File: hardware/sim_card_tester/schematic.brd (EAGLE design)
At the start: 160 x 100 mm, 146 parts, among them IC1 TPS6300, J2 MICRO_USB_B_HIROSE_ZX62R-B-5P, J3 CON_MICRO_SDDM3AT-SF-PEJM5, J4 NANO_SIM, J5 NANO_SIM, J6 TC2030-JLINK-NL, J7 NANO_SIM, J8 NANO_SIM, J9 U.FL-R-SMT, Q11 SI223DDS, Q3 MOSFET-NCHANNELSMD, Q4 MOSFET-NCHANNELSMD, Q5 MOSFET-NCHANNELSMD, U1 AB1815-T3, U10 SIP32510, U11 SIP32510, U14 SARA-U2, U15 MAX4734EUB+, U16 SARA-U2, U17 TXB0104RUT, U2 BGA725L6-ALT, U20 MAX4734EUB+, U21 MAX4734EUB+, U22 MAX4734EUB+, U3 FTDI234XD, U4 SAFFB1G56KB0F0A, U5 MAX8887EZK33+T, U6 MCP73831, U7 MAX-M8, U8 MAX67XXMAX6749MAX67XX, U9 NRF52840, X1 ABS07-32.768KHZ-7-T, X4 32MHz, X5 32.768kHz

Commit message: second pcb
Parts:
- removed C13: 33pF, passives:0603_CAP
- removed C15: 100uF, passives:0805_CAP
- removed C22, C24, C25, C26: 47pF, passives:0402_CAP
- removed C49: 56pF, passives:0402_CAP
- removed C50: 10nF, passives:0402_CAP
- removed C51: 100nF, passives:0402_CAP
- removed C52: 220uF, passives:1210_CAP
- removed D10, D11, D8, D9: 14V, passives:0402_DIODE
- removed J9: U.FL-R-SMT, connector:U.FL_SMT
- removed Q11: SI223DDS, fets:SOT23-3
- removed Q4, Q5: MOSFET-NCHANNELSMD, fets:SOT23-3
- removed R25: 10k, passives:0402_RES
- removed R36: 0, passives:0402_RES
- removed R40, R42: 100k, passives:0402_RES
- removed R45: 100, passives:0402_RES
- removed U14, U16: SARA-U2, ubloxLib:SARA-96
- removed U17: TXB0104RUT, chips:UQFN-12
- added C11, C12, C16, C28: 47pF, passives:0402_CAP
- added C17: 56pF, passives:0402_CAP
- added C18: 100uF, passives:0805_CAP
- added C19: 10nF, passives:0402_CAP
- added C20: 220uF, passives:1210_CAP
- added C21: 100nF, passives:0402_CAP
- added C27: 33pF, passives:0603_CAP
- added D3, D4, D6, D7: 14V, passives:0402_DIODE
- added J13: U.FL-R-SMT, connector:U.FL_SMT
- added Q2, Q6: MOSFET-NCHANNELSMD, fets:SOT23-3
- added Q7: SI223DDS, fets:SOT23-3
- added R10: 10k, passives:0402_RES
- added R43, R46: 100k, passives:0402_RES
- added R47: 0, passives:0402_RES
- added R48: 100, passives:0402_RES
- added U12: UBLOX_SARA_G350, signpost:UBLOX_SARA_G3
- added U13: TXB0104RUT, chips:UQFN-12
- moved U5 132.8 mm to (138.4, 78.7)
- moved C33 130.7 mm to (141.0, 81.3)
- moved R32 114.9 mm to (149.9, 96.5)
- moved JP1 112.4 mm to (151.1, 87.6)
- moved J2 107.0 mm to (118.1, 50.8)
- moved FB2 106.8 mm to (119.4, 61.0), turned to 90 degrees
- moved R9 102.9 mm to (61.0, 27.9)
- moved C5 94.8 mm to (115.6, 57.1)
- moved R1 93.0 mm to (110.5, 52.1)
- moved C4 85.3 mm to (110.5, 62.2)
- moved C43 84.7 mm to (25.4, 73.7)
- moved C42 81.1 mm to (20.3, 73.7)
- moved B1 79.6 mm to (120.7, 94.0)
- moved U3 75.0 mm to (105.4, 50.8), turned to 180 degrees
- moved C44 69.0 mm to (45.7, 68.6)
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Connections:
- removed net N$10: C13.2, R36.2
- removed net N$11: C13.1, U16.56
- removed net N$50: J9.SIG, R36.1
- removed net N$52: Q4.3, Q5.3, U16.9
- removed net N$54: Q4.2, U16.18
- removed net N$56: R42.2
- removed net N$57: Q5.2, U16.15
- removed net N$58: U16.10, U17.2
- removed net N$62: U16.11, U17.3
- removed net N$7: R25.1, U17.12
- removed net N$80: Q11.1, R45.1
- removed net N$95: C22.2, C24.2, C25.2, C26.2, D10.ANODE, D11.ANODE, D8.ANODE, D9.ANODE
- removed net RXD: U16.13, U17.5
- removed net TXD: U16.12, U17.4
- removed net VBCKP: C15.P$1, R42.1, U14.2
- removed net VSIM: U16.41
- removed net V_BCKP: U16.2
- removed net V_INT: U16.4
- new net 3V3: R10.2, U13.11
- new net N$12: U12.13, U13.5
- new net N$15: Q6.3, U12.18
- new net N$16: C18.P$1, R43.2, U12.2
- new net N$18: Q2.3, R43.1, U12.15
- new net N$25: U12.11, U13.3
- new net N$53: U12.10, U13.2
- new net N$63: C27.2, R47.1
- new net N$66: Q7.1, R48.1
- new net N$68: R10.1, U13.12
- new net N$69: C27.1, U12.56
- new net N$70: J13.SIG, R47.2
- new net N$71: C11.2, C12.2, C16.2, C28.2, D3.ANODE, D4.ANODE, D6.ANODE, D7.ANODE
- new net N$9: U12.12, U13.4
- net +3V3: no longer R25.2, U17.11
- net CLK_SIM: now also C28.1, D7.CATHODE, U12.38; no longer C26.1, D11.CATHODE, U14.38
- net GND: now also C17.2, C18.P$2, C19.2, C20.2, C21.2, J13.GND1, J13.GND2, Q2.2, Q6.2, R46.1, U12.1, U12.14, U12.20, U12.21, U12.22, U12.3, U12.30, U12.32, U12.33, U12.43, U12.5, U12.50, U12.54, U12.55, U12.57, U12.58, U12.59, U12.60, U12.61, U12.63, U12.64, U12.65, U12.66, U12.67, U12.68, U12.69, U12.70, U12.71, U12.72, U12.73, U12.74, U12.75, U12.76, U12.77, U12.78, U12.79, U12.80, U12.81, U12.82, U12.83, U12.84, U12.85, U12.86, U12.87, U12.88, U12.89, U12.9, U12.90, U12.91, U12.92, U12.93, U12.94, U12.95, U12.96, U13.6; no longer C15.P$2, C49.2, C50.2, C51.2, C52.2, J9.GND1, J9.GND2, R40.1, U14.1, U14.14, U14.20, U14.21, U14.22, U14.3, U14.30, U14.32, U14.43, U14.5, U14.50, U14.54, U14.55, U14.57, U14.58, U14.59, U14.60, U14.61, U14.63, U14.64, U14.65, U14.66, U14.67, U14.68, U14.69, U14.70, U14.71, U14.72, U14.73, U14.74, U14.75, U14.76, U14.77, U14.78, U14.79, U14.80, U14.81, U14.82, U14.83, U14.84, U14.85, U14.86, U14.87, U14.88, U14.89, U14.90, U14.91, U14.92, U14.93, U14.94, U14.95, U14.96, U16.1, U16.14, U16.20, U16.21, U16.22, U16.3, U16.30, U16.32, U16.43, U16.5, U16.50, U16.54, U16.55, U16.57, U16.58, U16.59, U16.60, U16.61, U16.63, U16.64, U16.65, U16.66, U16.67, U16.68, U16.69, U16.70, U16.71, U16.72, U16.73, U16.74, U16.75, U16.76, U16.77, U16.78, U16.79, U16.80, U16.81, U16.82, U16.83, U16.84, U16.85, U16.86, U16.87, U16.88, U16.89, U16.90, U16.91, U16.92, U16.93, U16.94, U16.95, U16.96, U17.6
- net GSM_3V8: now also Q7.2; no longer Q11.2
- net GSM_CTS: now also U13.10; no longer U17.10
- net GSM_GATED: now also C17.1, C19.1, C20.1, C21.1, Q7.3, U12.51, U12.52, U12.53; no longer C49.1, C50.1, C51.1, C52.1, Q11.3, U14.53
- net GSM_LED: now also U12.16; no longer U16.16
- net GSM_POWER: now also Q2.1; no longer Q5.1
- net GSM_POWER_GATE: now also R46.2, R48.2; no longer R40.2, R45.2
- net GSM_RST: now also Q6.1; no longer Q4.1
- net GSM_RTS: now also U13.9; no longer U17.9
- net GSM_RX: now also U13.8; no longer U17.8
- net GSM_TX: now also U13.7; no longer U17.7
- net IO_SIM: now also C11.1, D4.CATHODE, U12.39; no longer C22.1, D9.CATHODE, U14.39
- net RST_SIM: now also C12.1, D6.CATHODE, U12.40; no longer C24.1, D10.CATHODE, U14.40
- net VCC: no longer U14.51, U14.52, U16.51, U16.52, U16.53
- net VCC_SIM: now also C16.1, D3.CATHODE, U12.41; no longer C25.1, D8.CATHODE, U14.41
- net V_GSM_INT: now also U12.4, U13.1; no longer U14.4, U17.1
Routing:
- net GND: track 1200.7 -> 0.00 mm, vias 52 -> 0
- net N$17: track 195.8 -> 5.30 mm, vias 10 -> 0
- net N$51: track 198.8 -> 32.8 mm, vias 15 -> 0
- net BAT: track 185.1 -> 35.6 mm, vias 18 -> 2
- net GPS_VCC: track 221.9 -> 77.6 mm, vias 19 -> 6
- net !SD_DETECT: track 195.6 -> 59.3 mm, vias 19 -> 0
- net WDI: track 84.0 -> 219.1 mm, vias 2 -> 5
- net VCC: track 281.3 -> 167.5 mm, vias 28 -> 8
- net !NRF_CS_SD: track 165.9 -> 52.6 mm, vias 9 -> 4
- net MUX_SEL2: track 70.9 -> 181.0 mm, vias 9 -> 12
- net D+: track 123.0 -> 17.2 mm, vias 8 -> 2
- net N$27: track 106.2 -> 5.36 mm, vias 4 -> 0
- net N$46: track 107.2 -> 7.66 mm, vias 2 -> 0
- net N$48: track 101.9 -> 3.30 mm, vias 6 -> 0
- net RXD: track 93.9 -> 0.00 mm, vias 6 -> 0
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
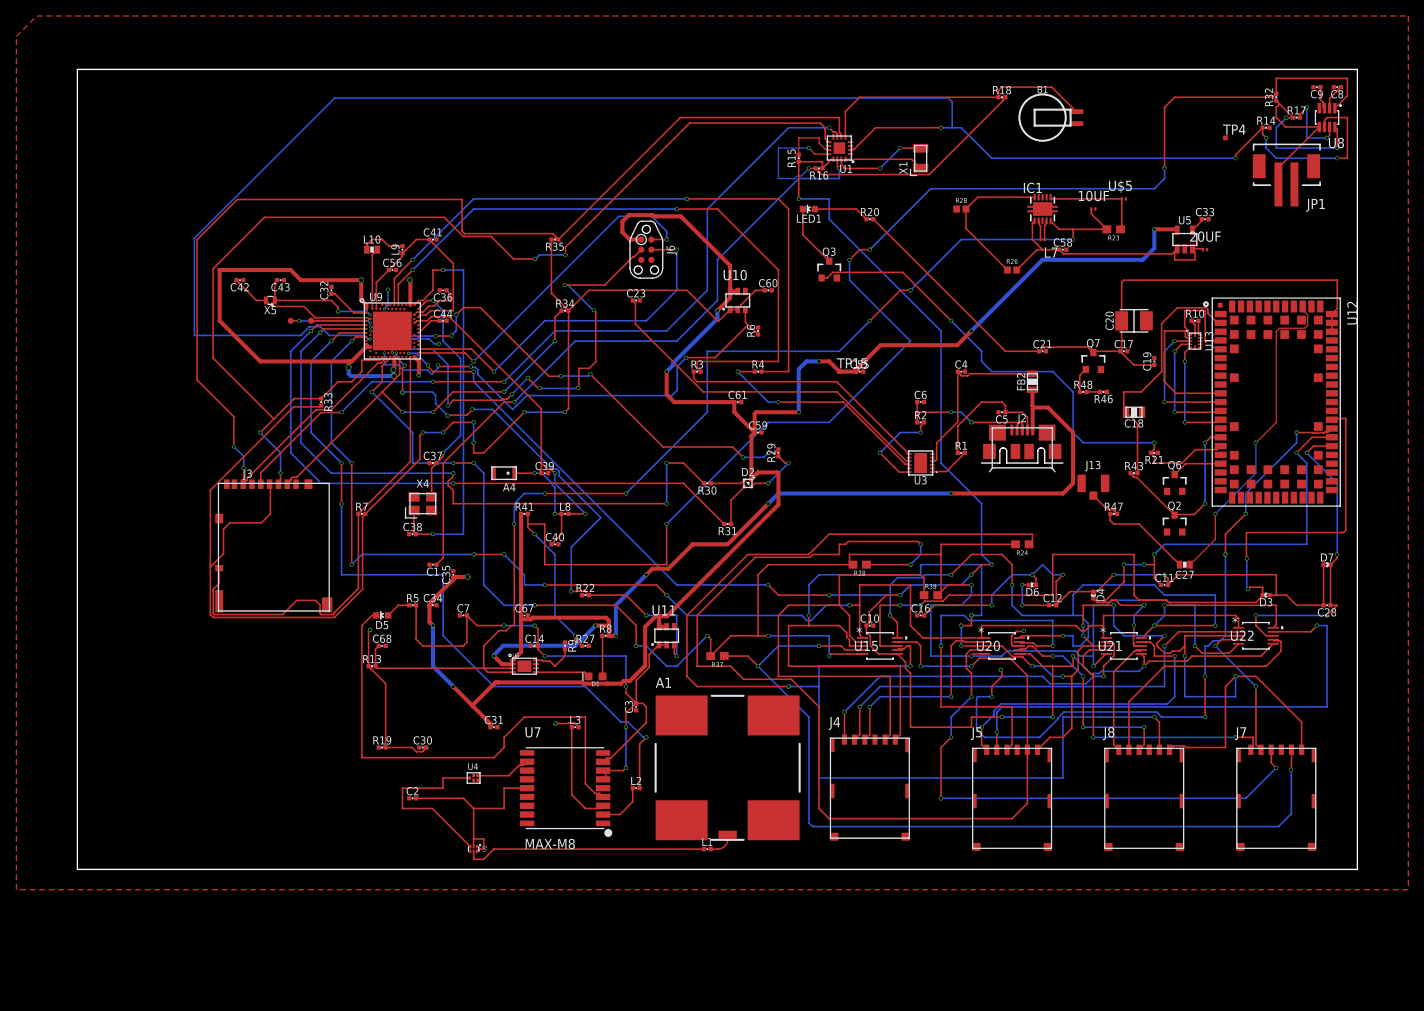
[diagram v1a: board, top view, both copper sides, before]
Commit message: fixed schematic and nrf routing
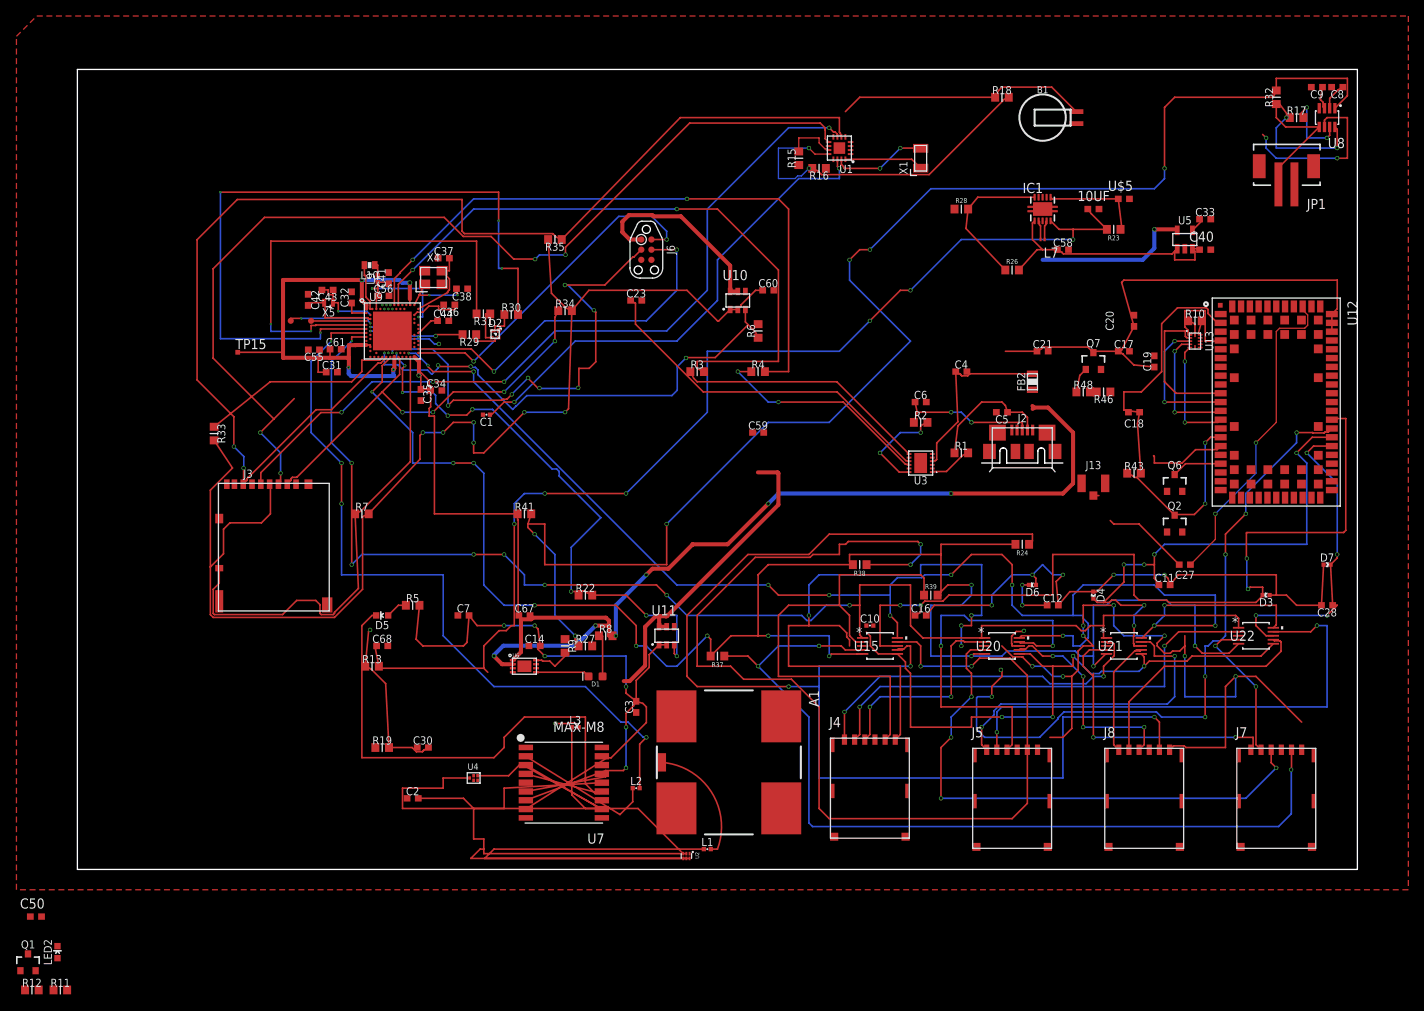
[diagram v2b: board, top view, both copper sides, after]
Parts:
- removed 20UF: (no value), Nordic_nRF:RESC0201_L
- removed A4: ANT3216A063R2400A, chips:ANT3216A063R2400A
- removed C39: 1pF, passives:0402_CAP
- removed L8: 3.9nH, passives:0402_CAP
- removed LED1: BLUE, leds:LED-0603
- removed Q3: MOSFET-NCHANNELSMD, fets:SOT23-3
- removed R14: 10k, passives:0402_RES
- removed R20: 1k, passives:0402_RES
- removed R21: 100k, passives:0402_RES
- removed R47: 0, passives:0402_RES
- removed TP4: TPTP06SQ, testpad:TP06SQ
- added C50: 10uF, Nordic_nRF:RESC0603_L
- added LED2: BLUE, leds:LED-0603
- added Q1: MOSFET-NCHANNELSMD, fets:SOT23-3
- added R11: 1k, BeagleBone_Black_Wireless:R0603
- added R12: 100k, BeagleBone_Black_Wireless:R0603
- 10UF: value (none) -> 10uF; device Nordic_nRF:RESC0201_L -> Nordic_nRF:RESC0603_L
- C11, C12, C14, C16, C17, C19, C2, C21, C23, C28, C3, C30, C31, C32, C33, C34, C35, C36, C37, C38, C4, C41, C42, C43, C44, C5, C55, C56, C58, C59, C6, C60, C61, C67, C68, C7, C8, C9: device passives:0402_CAP -> Nordic_nRF:RESC0603_L
- C18: device passives:0805_CAP -> Nordic_nRF:RESC0603_L
- C20: device passives:1210_CAP -> Nordic_nRF:RESC0603_L
- C27: device passives:0603_CAP -> Nordic_nRF:RESC0603_L
- C40: value 1pF -> 10uF; device passives:0402_CAP -> Nordic_nRF:RESC0603_L
- R1, R10, R13, R15, R16, R17, R18, R19, R2, R22, R27, R29, R3, R30, R31, R32, R33, R34, R35, R4, R41, R43, R46, R48, R5, R6, R7, R8, R9: device passives:0402_RES -> BeagleBone_Black_Wireless:R0603
- R23, R24, R37, R38, R39: device SparkFun-Resistors:0603 -> BeagleBone_Black_Wireless:R0603
- R26, R28: device SparkFun-Resistors:0402 -> BeagleBone_Black_Wireless:R0603
- U$5: device Nordic_nRF:RESC0201_L -> Nordic_nRF:RESC0603_L
- moved C40 89.2 mm to (141.0, 77.5)
- moved TP15 75.2 mm to (20.0, 64.6)
- moved C55 68.3 mm to (29.6, 65.0), turned to 180 degrees
- moved C61 50.7 mm to (32.3, 65.0)
- moved C31 48.8 mm to (31.8, 62.2)
- moved R29 41.4 mm to (49.0, 66.9), turned to 180 degrees
- moved R31 40.3 mm to (50.7, 69.4)
- moved D2 36.7 mm to (52.2, 66.9)
- moved R30 32.3 mm to (54.2, 69.4), turned to 0 degrees
- moved C38 31.3 mm to (48.1, 72.6), turned to 180 degrees
- moved X4 28.3 mm to (44.5, 74.0)
- moved C34 26.9 mm to (44.9, 59.9)
- moved U2 26.6 mm to (76.1, 1.68)
- moved C37 25.6 mm to (45.8, 76.4)
- moved C35 22.8 mm to (42.9, 59.3), turned to 270 degrees
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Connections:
- removed net 0: J4.C5, J5.C5, J7.C5, J8.C5, U15.3, U20.3, U21.3, U22.3
- removed net 3V3: R10.2, U13.11
- removed net 5V: C67.1, FB2.P$2, J2.1, R41.1, R8.2, U6.1, U6.2
- removed net CONNECT: 10UF.1, C68.1, IC1.5, R13.2, R23.2, U6.3, U6.4
- removed net GSM_3V8: Q7.2
- removed net N$30: IC1.3
- removed net N$37: IC1.9
- removed net N$38: C39.1, L8.2, U9.H23
- removed net N$42: A4.S1, C40.1, L8.1
- removed net N$44: LED1.C, Q3.3
- removed net N$49: LED1.A, R20.1
- removed net N$51: 20UF.1, C58.1, IC1.1, R26.2, U5.1, U5.3
- removed net N$63: C27.2, R47.1
- removed net RTC_CS: U9.U1
- removed net RTC_INT1: U9.AC11
- new net N$14: LED2.C, Q1.3
- new net N$23: LED2.A, R11.1
- net !EXTERNAL_RST: now also U9.AD20
- net !RTC_CS: now also U9.U1
- net !RTC_INT1: now also U9.AC11
- net +3V3: now also C10.1, C40.1, C50.1, C58.1, C67.1, IC1.1, Q7.2, R10.2, R15.1, R16.1, R26.2, R41.1, R8.2, U1.13, U13.11, U5.1, U5.3, U6.1, U6.2
- net BAT: now also 10UF.1, C68.1, IC1.5, R13.2, R23.2, U6.3, U6.4
- net BATIN: now also U9.R24; no longer U9.B9
- net GND: now also C18.2, C50.2, IC1.3, IC1.9, J4.C5, J5.C5, J7.C5, J8.C5, Q1.2, R12.1, U15.3, U20.3, U21.3, U22.3; no longer 20UF.2, A4.S2, C18.P$2, C39.2, Q3.2, R14.2, R21.1, TP4.TP
- net GSM_CTS: now also U9.A12
- net GSM_GATED: now also R11.2; no longer R20.2
- net GSM_LED: now also Q1.1, R12.2; no longer Q3.1, R21.2
- net GSM_POWER: now also U9.B13
- net GSM_RST: now also U9.A10
- net GSM_RTS: now also U9.B11
- net GSM_RX: now also U9.B9
- net GSM_TX: now also U9.A8
- net N$16: now also C18.1; no longer C18.P$1
- net N$70: now also C27.2; no longer R47.2
- net VCC: now also FB2.P$2, J2.1; no longer C10.1, R15.1, R16.1, U1.13
- net WDI: no longer R14.1, U1.2
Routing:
- net WDI: track 219.1 -> 21.5 mm, vias 5 -> 2
- net 0: track 194.1 -> 0.00 mm, vias 12 -> 0
- net GND: track 0.00 -> 173.4 mm, vias 0 -> 12
- net CONNECT: track 146.8 -> 0.00 mm, vias 6 -> 0
- net BAT: track 35.6 -> 174.0 mm, vias 2 -> 8
- net 5V: track 137.1 -> 0.00 mm, vias 6 -> 0
- net VCC: track 167.5 -> 78.8 mm, vias 8 -> 4
- net VCC_RF: track 25.2 -> 87.7 mm
- net GSM_LED: track 66.5 -> 10.1 mm, vias 2 -> 0
- net LED_NRF_RED: track 62.6 -> 12.2 mm, vias 8 -> 2
- net N$45: track 51.4 -> 8.53 mm
- net +3V3: track 322.8 -> 357.7 mm, vias 15 -> 12
- net N$51: track 32.8 -> 0.00 mm
- net N$38: track 40.1 -> 8.41 mm, vias 2 -> 1
- net GPS_VCC: track 77.6 -> 108.6 mm
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
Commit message: fixed most things
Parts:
- moved R12 185.2 mm to (152.9, 80.6), turned to 180 degrees
- moved Q1 177.0 mm to (146.4, 78.0)
- moved LED2 172.8 mm to (144.6, 80.4)
- moved R11 169.0 mm to (138.9, 78.1), turned to 180 degrees
- moved JP1 145.5 mm to (26.7, 12.1), turned to 180 degrees
- moved C33 140.0 mm to (13.4, 23.6)
- moved U5 139.7 mm to (12.0, 19.1)
- moved C40 136.5 mm to (17.9, 18.6)
- moved U$5 134.0 mm to (17.7, 12.0)
- moved 10UF 130.7 mm to (20.5, 6.83)
- moved IC1 130.3 mm to (14.6, 6.76)
- moved L7 129.9 mm to (14.6, 3.68)
- moved C58 129.8 mm to (9.60, 14.6)
- moved R23 128.6 mm to (18.4, 15.4), turned to 0 degrees
- moved R26 126.6 mm to (9.53, 7.72), turned to 180 degrees
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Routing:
- net GND: track 173.4 -> 0.25 mm, vias 12 -> 0
- net N$31: track 182.2 -> 16.6 mm, vias 6 -> 3
- net !RTC_CS: track 44.0 -> 202.4 mm, vias 2 -> 4
- net GSM_RST: track 0.00 -> 129.6 mm, vias 0 -> 1
- net N$55: track 158.4 -> 29.5 mm, vias 6 -> 0
- net GSM_POWER: track 0.00 -> 118.6 mm, vias 0 -> 1
- net GSM_TX: track 0.00 -> 116.9 mm, vias 0 -> 1
- net GSM_CTS: track 0.00 -> 102.8 mm, vias 0 -> 1
- net GSM_RX: track 0.00 -> 102.8 mm, vias 0 -> 1
- net GSM_RTS: track 0.00 -> 99.6 mm, vias 0 -> 1
- net VCC: track 78.8 -> 171.6 mm, vias 4 -> 6
- net BAT: track 174.0 -> 82.1 mm, vias 8 -> 0
- net GPS_VCC: track 108.6 -> 20.5 mm, vias 6 -> 0
- net VCC_RF: track 87.7 -> 5.96 mm
- net N$2: track 69.7 -> 4.21 mm
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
